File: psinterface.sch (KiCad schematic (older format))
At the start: 7 parts, among them J1 Conn_02x04_Top_Bottom, J2 Conn_01x10, J3 Conn_02x06_Top_Bottom, J4 Conn_01x05, J5 Conn_01x01, J6 Conn_01x03, SW1 SW_SPDT

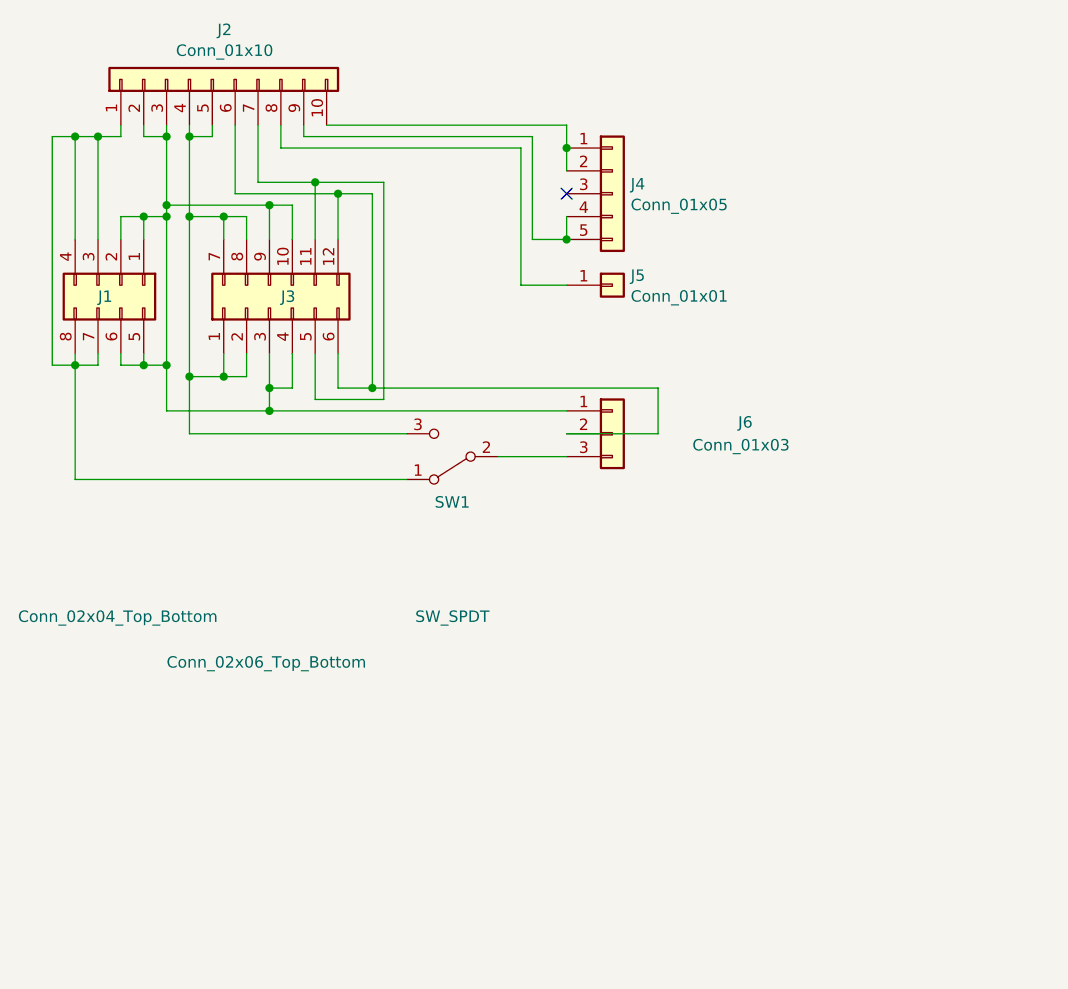
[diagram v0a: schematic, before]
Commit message: Reduced sized, added text labels
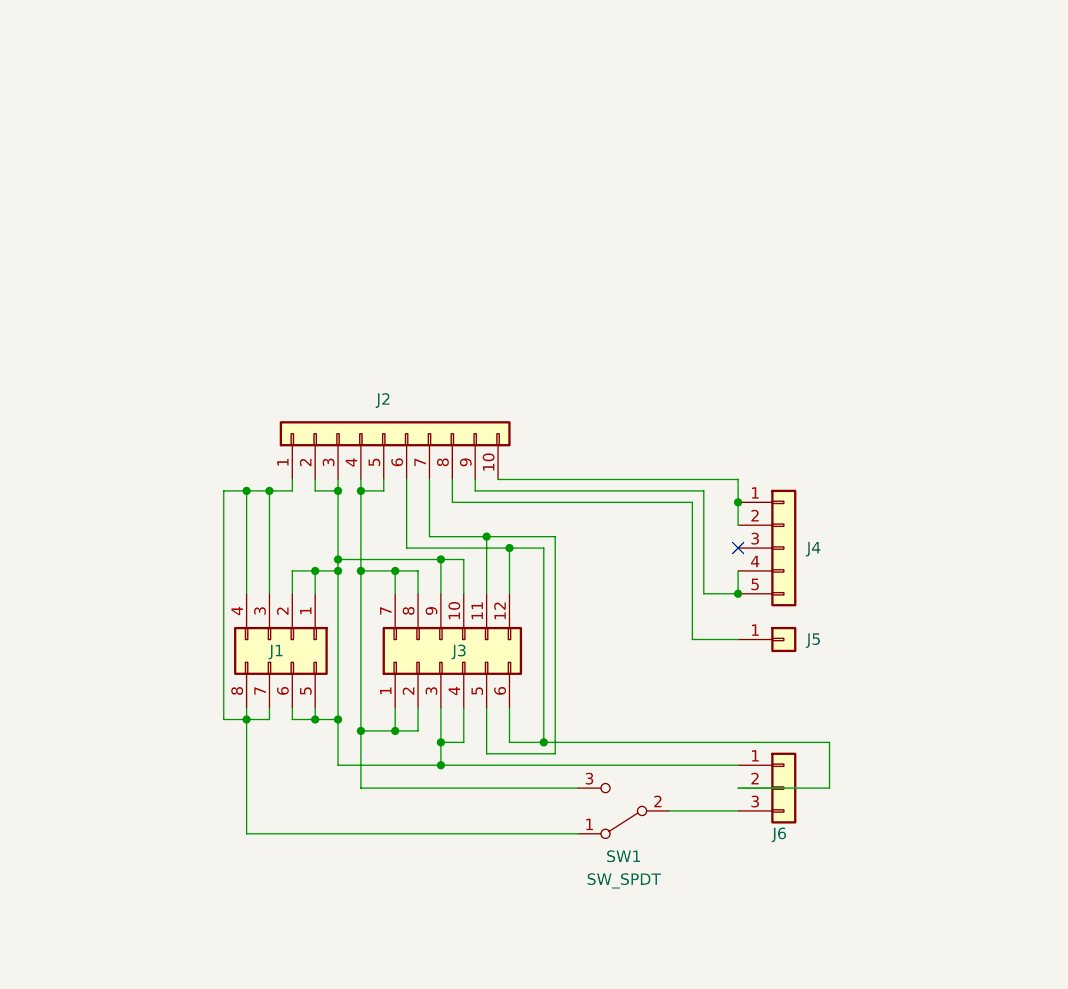
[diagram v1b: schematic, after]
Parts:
- J6: footprint Connector_PinHeader_2.54mm:PinHeader_1x03_P2.54mm_Vertical -> Connector_Wire:SolderWirePad_1x03_P3.175mm_Drill1mm
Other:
- moved on the sheet: J1, J2, J3, J4, J5, J6, SW1

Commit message: Corrected AC wiring, updated parts list
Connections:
- net at J2.10 (Pin_10), J4.1 (Pin_1): no longer J4.2 (Pin_2)
- net at J2.8 (Pin_8), J5.1 (Pin_1): now also J4.5 (Pin_5)
- net at J4.3 (Pin_3): now also J2.9 (Pin_9)
- now unconnected: J4.4 (Pin_4)
- no-connect marks 1 -> 2
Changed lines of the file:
@@
 Sheet 1 1
 Title "AWSD PS Interface"
-Date "2020-02-07"
-Rev "0.1"
+Date "2020-02-08"
+Rev "0.3"
 Comp ""
 Comment1 ""
@@
 $EndComp
 Wire Wire Line
-	6450 3800 6600 3800
-Wire Wire Line
 	4650 3300 4650 3350
 Wire Wire Line
@@
 Wire Wire Line
 	5450 3300 5450 3350
-Wire Wire Line
-	5450 3350 6450 3350
-Wire Wire Line
-	6450 3350 6450 3800
 $Comp
 L Connector_Generic:Conn_01x01 J5
@@
 	6400 3400 6400 4000
 Wire Wire Line
-	6400 4000 6600 4000
+	6400 4000 6500 4000
 $Comp
 L Connector_Generic:Conn_01x03 J6
@@
 Wire Wire Line
 	5750 4450 7000 4450
-NoConn ~ 6600 3600
 Wire Wire Line
 	6600 3300 6600 3400
 Wire Wire Line
-	6600 3500 6600 3400
-Connection ~ 6600 3400
-Wire Wire Line
-	6600 3700 6600 3800
-Connection ~ 6600 3800
+	6500 3350 6500 3600
+Wire Wire Line
+	6500 3600 6600 3600
+Wire Wire Line
+	5450 3350 6500 3350
+NoConn ~ 6600 3500
+NoConn ~ 6600 3700
+Wire Wire Line
+	6600 3800 6500 3800
+Wire Wire Line
+	6500 3800 6500 4000
+Connection ~ 6500 4000
+Wire Wire Line
+	6500 4000 6600 4000
 $EndSCHEMATC

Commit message: Mounting holes for LCD fixed
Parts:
- added H1, H2: MountingHole, MountingHole:MountingHole_2.7mm_M2.5, symbol Mechanical:MountingHole
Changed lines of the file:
@@
 Wire Wire Line
 	6500 4000 6600 4000
+$Comp
+L Mechanical:MountingHole H1
+U 1 1 5E3FD440
+P 4500 5100
+F 0 "H1" H 4600 5146 50  0000 L CNN
+F 1 "MountingHole" H 4600 5055 50  0000 L CNN
+F 2 "MountingHole:MountingHole_2.7mm_M2.5" H 4500 5100 50  0001 C CNN
+F 3 "~" H 4500 5100 50  0001 C CNN
+	1    4500 5100
+	1    0    0    -1
+$EndComp
+$Comp
+L Mechanical:MountingHole H2
+U 1 1 5E3FEA25
+P 4500 5350
+F 0 "H2" H 4600 5396 50  0000 L CNN
+F 1 "MountingHole" H 4600 5305 50  0000 L CNN
+F 2 "MountingHole:MountingHole_2.7mm_M2.5" H 4500 5350 50  0001 C CNN
+F 3 "~" H 4500 5350 50  0001 C CNN
+	1    4500 5350
+	1    0    0    -1
+$EndComp
 $EndSCHEMATC

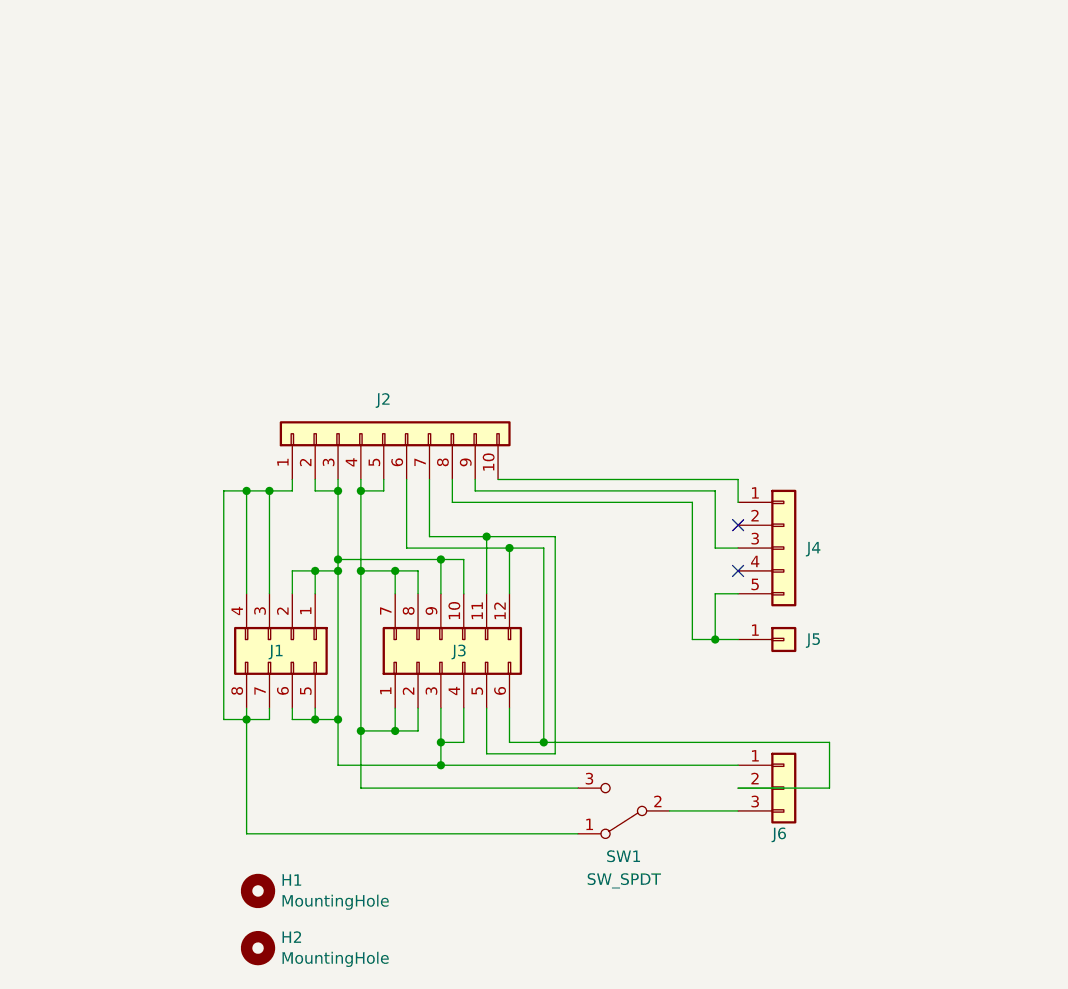
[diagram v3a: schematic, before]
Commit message: Rounded flanges, fixed wiring
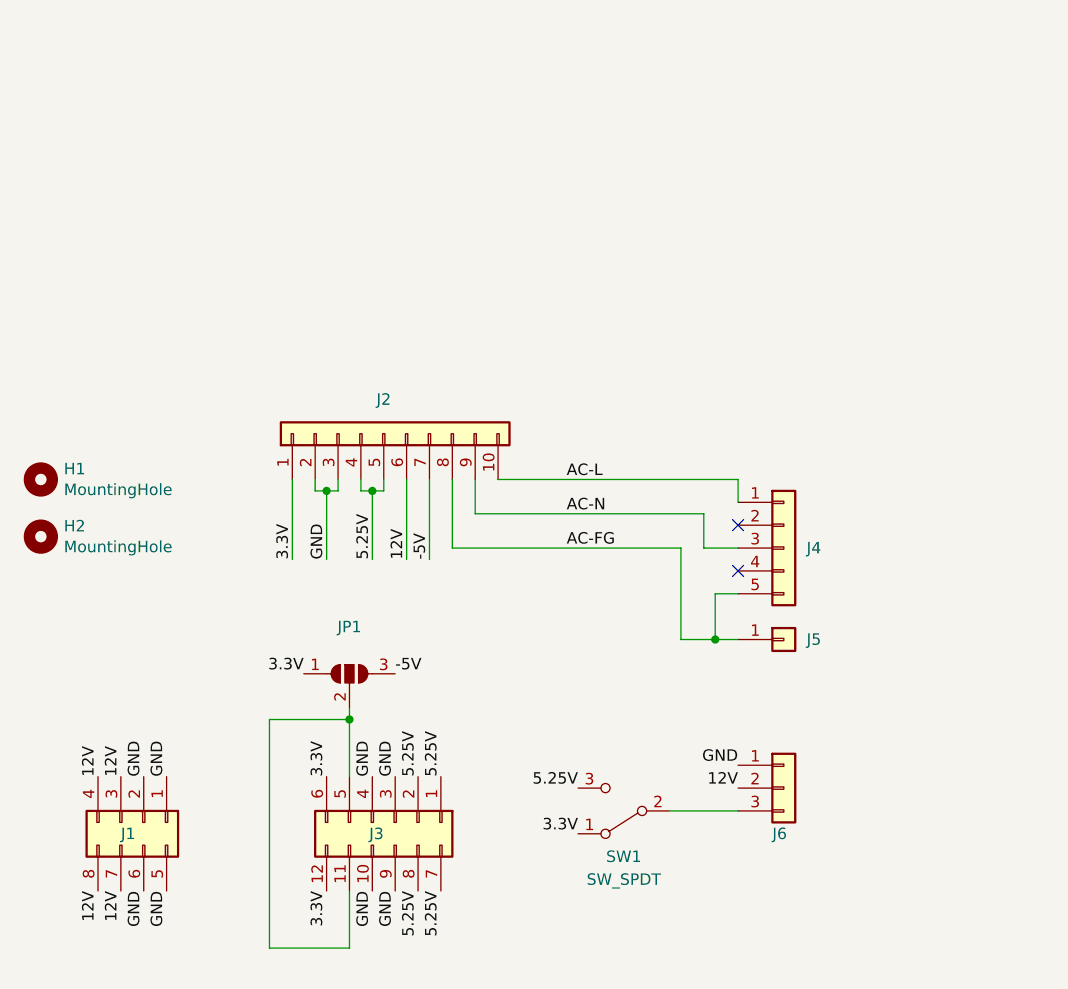
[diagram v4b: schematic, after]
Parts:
- added JP1: SolderJumper_3_Open, Andrew-Custom:SolderJumper-3_P3.5mm_Open_Pad3.0x3.0mm, symbol Jumper:SolderJumper_3_Open
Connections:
- net 5.25V: now reaches J2.4 (Pin_4), J2.5 (Pin_5), J3.1 (Pin_1), J3.2 (Pin_2), J3.7 (Pin_7), J3.8 (Pin_8), SW1.3 (C)
- net GND: now reaches J1.1 (Pin_1), J1.2 (Pin_2), J1.5 (Pin_5), J1.6 (Pin_6), J2.2 (Pin_2), J2.3 (Pin_3), J3.10 (Pin_10), J3.3 (Pin_3), J3.4 (Pin_4), J3.9 (Pin_9), J6.1 (Pin_1)
- net at J3.11 (Pin_11), J3.5 (Pin_5): now also JP1.2 (C); no longer J2.7 (Pin_7)
- net 12V: now reaches J2.6 (Pin_6), J6.2 (Pin_2)
- net 12V: now also J1.3 (Pin_3), J1.4 (Pin_4), J1.7 (Pin_7), J1.8 (Pin_8); no longer J3.12 (Pin_12), J3.6 (Pin_6)
- net AC-L: now reaches J2.10 (Pin_10), J4.1 (Pin_1)
- net AC-FG: now reaches J2.8 (Pin_8), J4.5 (Pin_5), J5.1 (Pin_1)
- net AC-N: now reaches J2.9 (Pin_9), J4.3 (Pin_3)
- new net -5V: J2.7 (Pin_7), JP1.3 (B)
- new net 3.3V: J2.1 (Pin_1), J3.12 (Pin_12), J3.6 (Pin_6), JP1.1 (A), SW1.1 (A)
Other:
- moved on the sheet: H1, H2, J1, J3

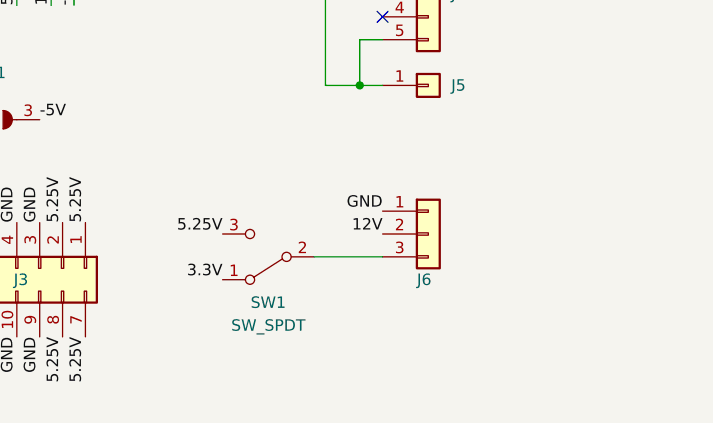
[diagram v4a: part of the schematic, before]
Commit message: J6 now 4MM, JP2/3 added to allow diff polarity LCD
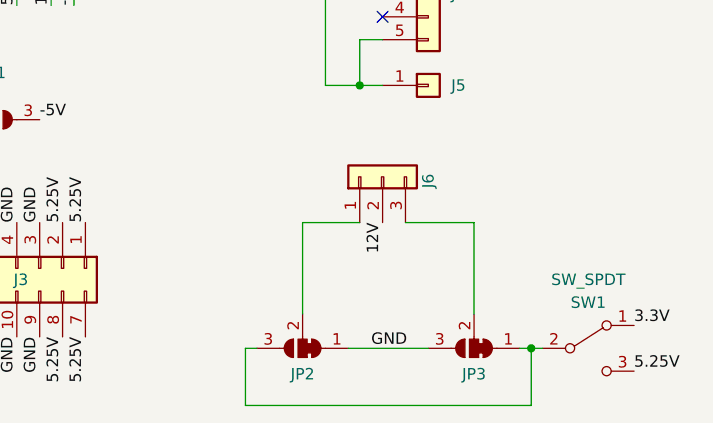
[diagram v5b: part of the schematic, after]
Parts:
- added JP2, JP3: SolderJumper_3_Bridged12, Jumper:SolderJumper-3_P1.3mm_Bridged12_RoundedPad1.0x1.5mm, symbol Jumper:SolderJumper_3_Bridged12
- J5: footprint MountingHole:MountingHole_3.2mm_M3_Pad_Via -> MountingHole:MountingHole_4.3mm_M4_Pad_Via
- J6: footprint Connector_Wire:SolderWirePad_1x03_P3.175mm_Drill1mm -> Connector_PinHeader_2.54mm:PinHeader_1x03_P2.54mm_Vertical
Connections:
- net GND: now also JP2.1 (A), JP3.3 (B); no longer J6.1 (Pin_1)
- net at J6.3 (Pin_3): now also JP3.2 (C); no longer SW1.2 (B)
- new net: J6.1 (Pin_1), JP2.2 (C)
- new net: JP2.3 (B), JP3.1 (A), SW1.2 (B)
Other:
- moved on the sheet: J6, SW1
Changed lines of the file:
@@
 Sheet 1 1
 Title "AWSD PS Interface"
-Date "2020-02-08"
-Rev "0.3"
+Date "2020-03-03"
+Rev "0.4"
 Comp ""
 Comment1 ""
@@
 F 0 "J5" H 6900 4000 50  0000 L CNN
 F 1 "Conn_01x01" H 6880 3951 50  0001 L CNN
-F 2 "MountingHole:MountingHole_3.2mm_M3_Pad_Via" H 6800 4000 50  0001 C CNN
+F 2 "MountingHole:MountingHole_4.3mm_M4_Pad_Via" H 6800 4000 50  0001 C CNN
 F 3 "~" H 6800 4000 50  0001 C CNN
 	1    6800 4000
@@
 L Connector_Generic:Conn_01x03 J6
 U 1 1 5E3F337E
-P 6800 4650
-F 0 "J6" H 6750 4450 50  0000 L CNN
-F 1 "Conn_01x03" H 7150 4600 50  0001 L CNN
-F 2 "Connector_Wire:SolderWirePad_1x03_P3.175mm_Drill1mm" H 6800 4650 50  0001 C CNN
-F 3 "~" H 6800 4650 50  0001 C CNN
-	1    6800 4650
-	1    0    0    -1
+P 6600 4400
+F 0 "J6" H 6550 4200 50  0000 L CNN
+F 1 "Conn_01x03" H 6950 4350 50  0001 L CNN
+F 2 "Connector_PinHeader_2.54mm:PinHeader_1x03_P2.54mm_Vertical" H 6600 4400 50  0001 C CNN
+F 3 "~" H 6600 4400 50  0001 C CNN
+	1    6600 4400
+	0    -1   -1   0
 $EndComp
 $Comp
 L Switch:SW_SPDT SW1
 U 1 1 5E3F57A9
-P 6100 4750
-F 0 "SW1" H 6100 4950 50  0000 C CNN
-F 1 "SW_SPDT" H 6100 5050 50  0000 C CNN
-F 2 "Button_Switch_THT:SW_CuK_OS102011MA1QN1_SPDT_Angled" H 6100 4750 50  0001 C CNN
-F 3 "~" H 6100 4750 50  0001 C CNN
-	1    6100 4750
-	-1   0    0    1
-$EndComp
-Wire Wire Line
-	6600 4750 6300 4750
+P 7500 5150
+F 0 "SW1" H 7500 5350 50  0000 C CNN
+F 1 "SW_SPDT" H 7500 5450 50  0000 C CNN
+F 2 "Button_Switch_THT:SW_CuK_OS102011MA1QN1_SPDT_Angled" H 7500 5150 50  0001 C CNN
+F 3 "~" H 7500 5150 50  0001 C CNN
+	1    7500 5150
+	1    0    0    -1
+$EndComp
 NoConn ~ 6600 3500
 NoConn ~ 6600 3700
@@
 Wire Wire Line
 	4550 5350 4900 5350
-Text Label 5900 4650 2    50   ~ 0
-5.25V
-Text Label 5900 4850 2    50   ~ 0
-3.3V
-Text Label 6600 4550 2    50   ~ 0
-GND
-Text Label 6600 4650 2    50   ~ 0
+Text Label 7700 5250 0    50   ~ 0
+5.25V
+Text Label 7700 5050 0    50   ~ 0
+3.3V
+Text Label 6600 4600 3    50   ~ 0
 12V
 Wire Wire Line
@@
 Wire Wire Line
 	4900 5350 4900 5100
+$Comp
+L Jumper:SolderJumper_3_Bridged12 JP3
+U 1 1 5E5FA165
+P 7000 5150
+F 0 "JP3" H 7000 5263 50  0000 C CNN
+F 1 "SolderJumper_3_Bridged12" H 7000 5264 50  0001 C CNN
+F 2 "Jumper:SolderJumper-3_P1.3mm_Bridged12_RoundedPad1.0x1.5mm" H 7000 5150 50  0001 C CNN
+F 3 "~" H 7000 5150 50  0001 C CNN
+	1    7000 5150
+	-1   0    0    1
+$EndComp
+$Comp
+L Jumper:SolderJumper_3_Bridged12 JP2
+U 1 1 5E5FC726
+P 6250 5150
+F 0 "JP2" H 6250 5263 50  0000 C CNN
+F 1 "SolderJumper_3_Bridged12" H 6250 5264 50  0001 C CNN
+F 2 "Jumper:SolderJumper-3_P1.3mm_Bridged12_RoundedPad1.0x1.5mm" H 6250 5150 50  0001 C CNN
+F 3 "~" H 6250 5150 50  0001 C CNN
+	1    6250 5150
+	-1   0    0    1
+$EndComp
+Text Label 6550 5150 0    50   ~ 0
+GND
+Wire Wire Line
+	6800 5150 6450 5150
+Wire Wire Line
+	7000 5000 7000 4600
+Wire Wire Line
+	7000 4600 6700 4600
+Wire Wire Line
+	6500 4600 6250 4600
+Wire Wire Line
+	6250 4600 6250 5000
+Wire Wire Line
+	7300 5150 7250 5150
+Wire Wire Line
+	7250 5150 7250 5400
+Wire Wire Line
+	7250 5400 6000 5400
+Wire Wire Line
+	6000 5400 6000 5150
+Wire Wire Line
+	6000 5150 6050 5150
+Connection ~ 7250 5150
+Wire Wire Line
+	7250 5150 7200 5150
 $EndSCHEMATC
